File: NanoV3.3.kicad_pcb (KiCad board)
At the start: 2 copper layers, 43.2 x 17.8 mm, 32 parts, among them IC1 FT232RL, IC2 LM1117IMPX-5.0, IC3 328P-MUR, J1 Conn_1x15, J2 Conn_1x15, J3 Conn_Mini_USB, J4 Conn_2x3, SW1 RESET, Y1 16MHz

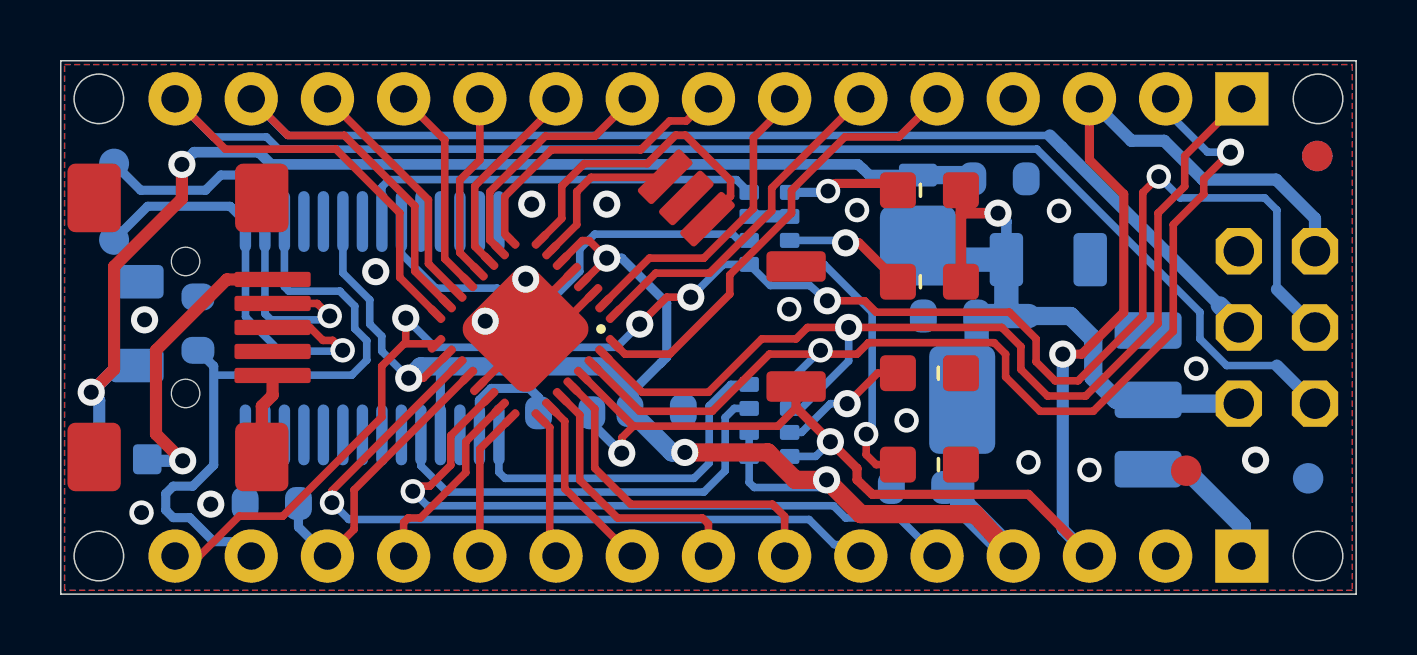
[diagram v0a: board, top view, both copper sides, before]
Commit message: Add silkscreen
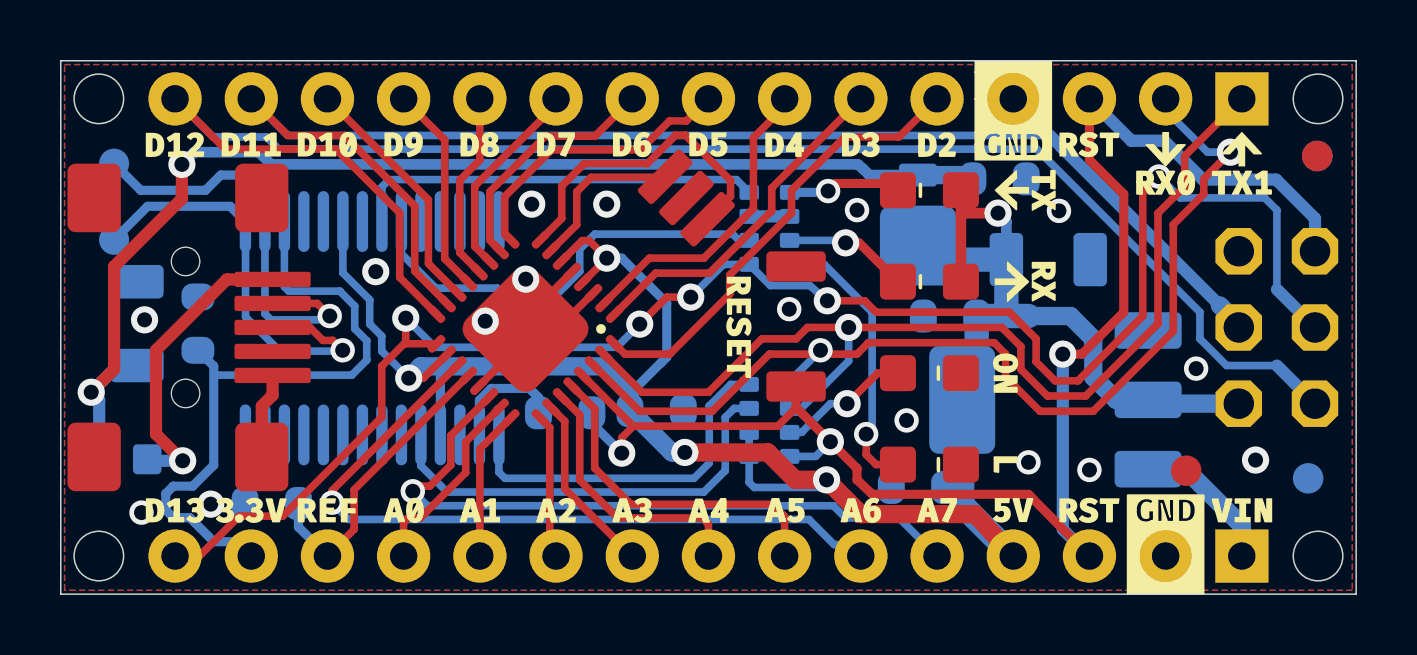
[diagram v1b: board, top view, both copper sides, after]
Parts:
- added Silkscreen_Back: Silkscreen_Front, NanoV3.3:Silkscreen_Back, B.Cu at (147.3, 101.6)
- added Silkscreen_Front: Silkscreen_Back, NanoV3.3:Silkscreen_Front, F.Cu at (147.3, 101.6)
